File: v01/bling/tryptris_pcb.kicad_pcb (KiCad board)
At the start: 2 copper layers, 298.8 x 122 mm, 226 parts, among them J1 USB_C_Receptacle_USB2.0, J2 I2C-L, J3 I2C-R, J4 AVR-ISP-6, SW1 Reset, U1 ATmega32U4-AU, U2 MCP23017_SO, U3 IS31FL3733-TQ, U4 HOLE, U4 IS31FL3733-TQ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

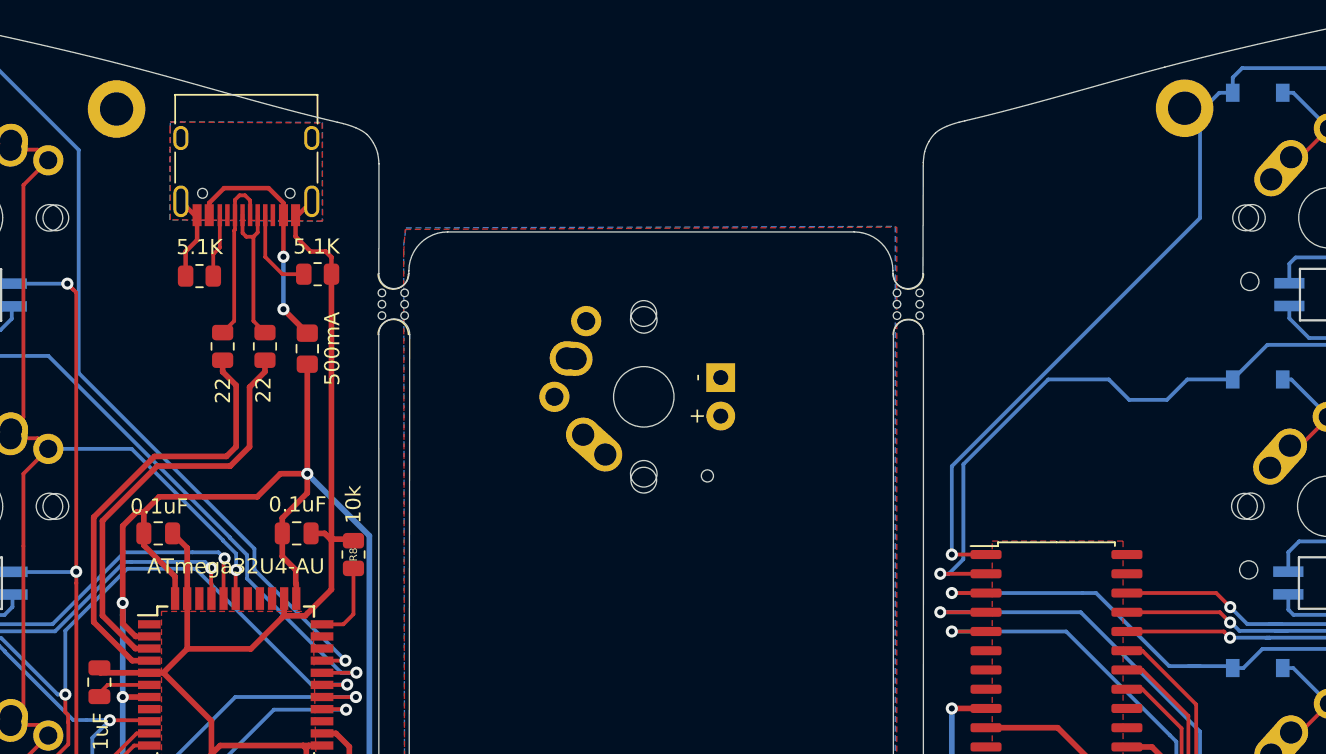
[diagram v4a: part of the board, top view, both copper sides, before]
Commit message: Add ESD component to both boards.
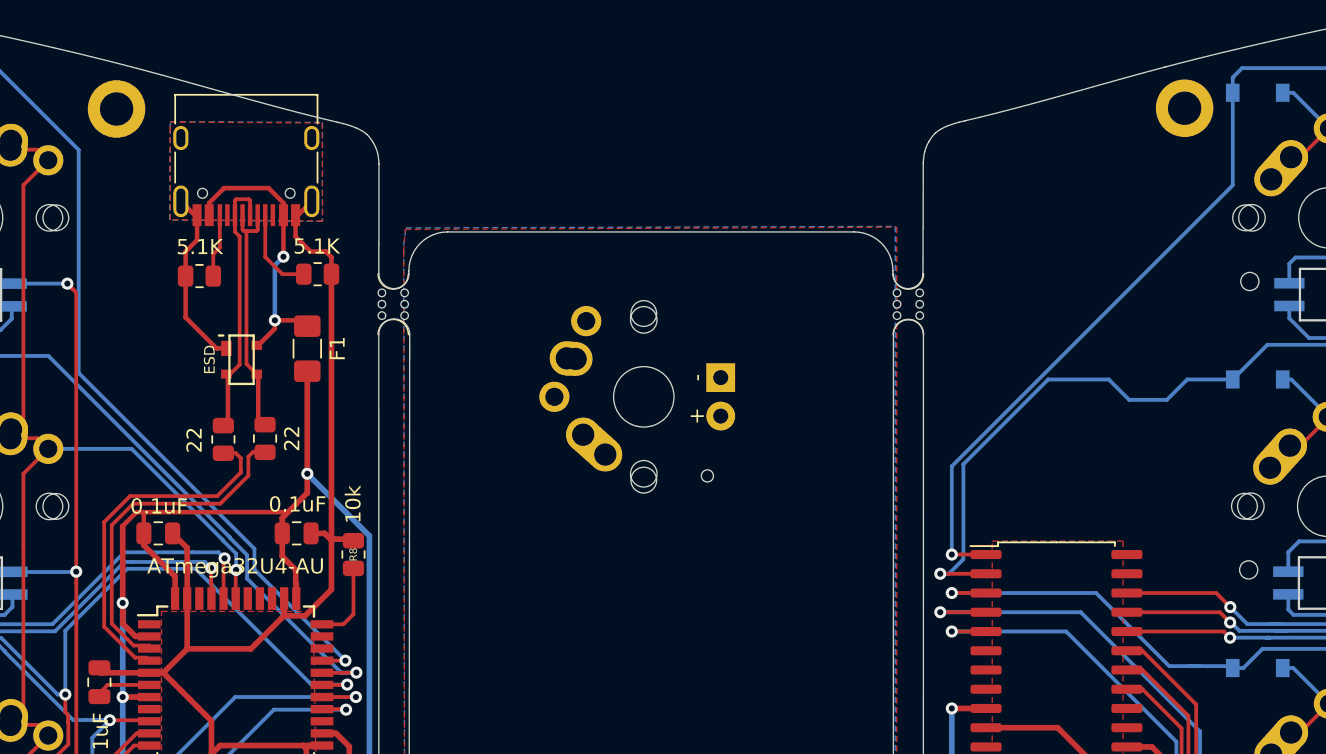
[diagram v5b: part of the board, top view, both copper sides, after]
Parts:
- added U5: PRTR5V0U2X, Keebio-Parts:SOT-143B, F.Cu at (148.9, 54.5)
- F1: footprint Fuse:Fuse_0805_2012Metric_Pad1.15x1.40mm_HandSolder -> Fuse:Fuse_1206_3216Metric_Pad1.42x1.75mm_HandSolder
- moved R5 6.14 mm to (147.8, 59.7), turned to 90 degrees
- moved R4 6.08 mm to (150.5, 59.6)
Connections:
- net Net-(J1-PadA7) renamed DN
- J1 pad A6: Net-(J1-PadA6) -> DP
- J1 pad B6: Net-(J1-PadA6) -> DP
- R5 pad 1: Net-(J1-PadA6) -> D+
- R5 pad 2: D+ -> DP
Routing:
- net DP: track 0.00 -> 17.7 mm
- net Net-(J1-PadA6): track 11.3 -> 0.00 mm
- net GND: track 302.7 -> 309.1 mm
- net DN: track 10.2 -> 16.3 mm
- net D+: track 29.1 -> 23.5 mm
- net D-: track 28.3 -> 23.2 mm
- net VCC: track 16.2 -> 19.0 mm
- net +5V: track 270.6 -> 268.6 mm
- net Row0-R: track 147.5 -> 146.9 mm

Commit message: Tweak routing on bling and add copper fill on left side
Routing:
- net Row1-R: track 142.2 -> 226.1 mm
- net Col2: track 174.2 -> 160.8 mm, vias 3 -> 2
- net Left-SW8: track 192.8 -> 196.2 mm
- net Row3-R: track 149.4 -> 151.3 mm
- net Col8: track 185.8 -> 187.1 mm
- net Right-SW6: track 145.3 -> 146.0 mm
- net SCL-R: track 163.9 -> 163.1 mm
- net Left-SW9: track 175.5 -> 176.2 mm
- net Row1-L: track 151.6 -> 152.2 mm
- net GND: vias 5 -> 87
